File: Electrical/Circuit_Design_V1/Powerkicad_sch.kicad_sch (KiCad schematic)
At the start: 0 parts

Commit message: #3 Creating power sub-schematic.
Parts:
- added C1: 1uF, symbol Device:C
- added P1: ~, symbol Etchasketch_hardware_symbol_library:20mm_Coin_Cell_Breakout_Board_(CR2032)
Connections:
- new net +3V3: C1.2, P1.1 (3V)
- new net GND: C1.1, P1.2 (GND)
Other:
- company: (none) -> AdrianTheHacker
- title: (none) -> Power

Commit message: #3 Sourcing capacitors, and designing power for MCU.
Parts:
- C1: Digikey Part Number (none) -> 3372-0603B105K100XDTR-ND
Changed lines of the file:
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@@
 			)
 		)
-		(property "Datasheet" "https://www.digikey.ca/en/products/detail/nextgen-components/0603B105K250XD/14670931"
+		(property "Datasheet" "https://mm.digikey.com/Volume0/opasdata/d220001/medias/docus/6482/3372_0603B105K100XD.pdf"
 			(at 149.86 113.03 0)
 			(effects
@@
 			)
 		)
-		(property "Description" "0603B105K250XD 1uF Ceramic Capacitor (25V)"
+		(property "Description" "1 µF ±10% 10V Ceramic Capacitor X7R 0603 (1608 Metric)"
 			(at 149.86 113.03 0)
 			(effects
 				(font
+					(size 1.27 1.27)
+				)
+				(hide yes)
+			)
+		)
+		(property "Digikey Part Number" "3372-0603B105K100XDTR-ND"
+			(at 149.86 113.03 90)
+			(effects
+				(font

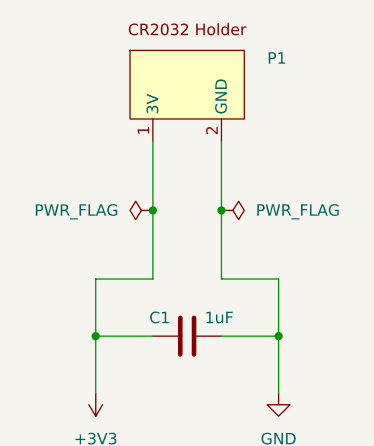
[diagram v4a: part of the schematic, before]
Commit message: #3 Making symbols.
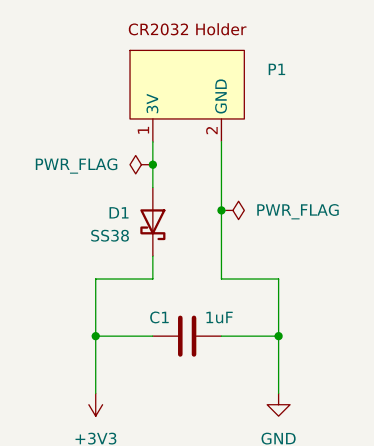
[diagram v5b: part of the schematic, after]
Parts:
- added D1: SS38, Diode_SMD:D_SMA, symbol Diode:SS38
- C1: footprint (none) -> Capacitor_SMD:C_0603_1608Metric
- P1: footprint (none) -> Etchasketch_Footprints:Coincell_Battery_Holder
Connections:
- net +3V3: now also D1.1 (K); no longer P1.1 (3V)
- new net: D1.2 (A), P1.1 (3V)
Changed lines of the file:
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@@
-	)
-	(junction
-		(at 146.05 99.06)
-		(diameter 0)
-		(color 0 0 0 0)
 	)
 	(junction
@@
 	)
 	(junction
+		(at 146.05 93.98)
+		(diameter 0)
+		(color 0 0 0 0)
+	)
+	(junction
 		(at 139.7 113.03)
 		(diameter 0)
@@
 	(wire
 		(pts
+			(xy 146.05 104.14) (xy 146.05 106.68)
+		)
+		(stroke
+			(width 0)
+			(type default)
+		)
+	)
+	(wire
+		(pts
 			(xy 139.7 106.68) (xy 139.7 113.03)
 		)
@@
 	(wire
 		(pts
+			(xy 146.05 93.98) (xy 146.05 91.44)
+		)
+		(stroke
+			(width 0)
+			(type default)
+		)
+	)
+	(wire
+		(pts
 			(xy 160.02 113.03) (xy 160.02 119.38)
 		)
@@
 	(wire
 		(pts
-			(xy 146.05 106.68) (xy 146.05 99.06)
-		)
-		(stroke
-			(width 0)
-			(type default)
-		)
-	)
-	(wire
-		(pts
-			(xy 146.05 99.06) (xy 146.05 91.44)
+			(xy 146.05 93.98) (xy 146.05 96.52)
 		)
 		(stroke
@@
 			)
 		)
-		(property "Footprint" ""
+		(property "Footprint" "Capacitor_SMD:C_0603_1608Metric"
 			(at 146.05 113.9952 0)
 			(effects
@@
 	(symbol
 		(lib_id "power:PWR_FLAG")
-		(at 146.05 99.06 90)
+		(at 146.05 93.98 90)
 		(unit 1)
 		(exclude_from_sim no)
@@
 		(fields_autoplaced yes)
 		(property "Reference" "#FLG01"
-			(at 144.145 99.06 0)
+			(at 144.145 93.98 0)
 			(effects
 				(font
@@
 		)
 		(property "Value" "PWR_FLAG"
-			(at 142.24 99.0599 90)
+			(at 142.24 93.9799 90)
 			(effects
 				(font
@@
 		)
 		(property "Footprint" ""
-			(at 146.05 99.06 0)
+			(at 146.05 93.98 0)
 			(effects
 				(font
@@
 		)
 		(property "Datasheet" "~"
-			(at 146.05 99.06 0)
+			(at 146.05 93.98 0)
 			(effects
 				(font
@@
 		)
 		(property "Description" "Special symbol for telling ERC where power comes from"
-			(at 146.05 99.06 0)
+			(at 146.05 93.98 0)
 			(effects
 				(font
@@
 	)
 	(symbol
+		(lib_id "Etchasketch_hardware_symbol_library:20mm_Coin_Cell_Breakout_Board_(CR2032)")
+		(at 149.86 88.9 0)
+		(unit 1)
+		(exclude_from_sim no)
+		(in_bom yes)
+		(on_board yes)
+		(dnp no)
+		(fields_autoplaced yes)
+		(property "Reference" "P1"
+			(at 158.75 83.4361 0)
+			(effects
+				(font
+					(size 1.27 1.27)
+				)
+				(justify left)
+			)
+		)
+		(property "Value" "~"
+			(at 149.86 88.9 0)
+			(effects
+				(font
+					(size 1.27 1.27)
+				)
+				(hide yes)
+			)
+		)
+		(property "Footprint" "Etchasketch_Footprints:Coincell_Battery_Holder"
+			(at 149.86 88.9 0)
+			(effects
+				(font
+					(size 1.27 1.27)
+				)
+				(hide yes)
+			)
+		)
+		(property "Datasheet" "https://www.te.com/commerce/DocumentDelivery/DDEController?Action=srchrtrv&DocNm=BAT-HLD-001&DocType=Data+Sheet&DocLang=English&DocFormat=pdf&PartCntxt=BAT-HLD-001"
+			(at 150.876 75.946 0)
+			(effects
+				(font
+					(size 1.27 1.27)
+				)
+				(hide yes)
+			)
+		)
+		(property "Description" "Coincell battery holder"
+			(at 149.352 73.406 0)
+			(effects
+				(font
+					(size 1.27 1.27)
+				)
+				(hide yes)
+			)
+		)
+		(pin "1"
+		)
+		(pin "2"
+		)
+		(instances
+			(project ""
+				(path "/40e3562c-f358-42bb-8418-a7c96a575201/7c7c338d-bf18-45a4-ba84-dd266c3ba486"
+					(reference "P1")
+					(unit 1)
+				)
+			)
+		)
+	)
+	(symbol
 		(lib_id "power:GND")
 		(at 160.02 119.38 0)
@@
 				(path "/40e3562c-f358-42bb-8418-a7c96a575201/7c7c338d-bf18-45a4-ba84-dd266c3ba486"
 					(reference "#PWR02")
-					(unit 1)
-				)
-			)
-		)
-	)
-	(symbol
-		(lib_id "Etchasketch_hardware_symbol_library:20mm_Coin_Cell_Breakout_Board_(CR2032)")
-		(at 149.86 88.9 0)
-		(unit 1)
-		(exclude_from_sim no)
-		(in_bom yes)
-		(on_board yes)
-		(dnp no)
-		(fields_autoplaced yes)
-		(property "Reference" "P1"
-			(at 158.75 82.1661 0)
-			(effects
-				(font
-					(size 1.27 1.27)
-				)
-				(justify left)
-			)
-		)
-		(property "Value" "~"
-			(at 158.75 84.7061 0)
-			(effects
-				(font
-					(size 1.27 1.27)
-				)
-				(justify left)
-			)
-		)
-		(property "Footprint" ""
-			(at 149.86 88.9 0)
-			(effects
-				(font
-					(size 1.27 1.27)
-				)
-				(hide yes)
-			)
-		)
-		(property "Datasheet" "https://www.te.com/commerce/DocumentDelivery/DDEController?Action=srchrtrv&DocNm=BAT-HLD-001&DocType=Data+Sheet&DocLang=English&DocFormat=pdf&PartCntxt=BAT-HLD-001"
-			(at 150.876 75.946 0)
-			(effects
-				(font
-					(size 1.27 1.27)
-				)
-				(hide yes)
-			)
-		)
-		(property "Description" "Coincell battery holder"
-			(at 149.352 73.406 0)
-			(effects
-				(font
-					(size 1.27 1.27)
-				)
-				(hide yes)
-			)
-		)
-		(pin "1"
-		)
-		(pin "2"
-		)
-		(instances
-			(project ""
-				(path "/40e3562c-f358-42bb-8418-a7c96a575201/7c7c338d-bf18-45a4-ba84-dd266c3ba486"
-					(reference "P1")
 					(unit 1)
 				)
@@
 					(unit 1)
 				)
+			)
+		)
+	)
+	(symbol
+		(lib_id "Diode:SS38")
+		(at 146.05 100.33 270)
+		(mirror x)
+		(unit 1)
+		(exclude_from_sim no)
+		(in_bom yes)
+		(on_board yes)
+		(dnp no)
+		(property "Reference" "D1"
+			(at 143.51 99.3774 90)
+			(effects
+				(font
+					(size 1.27 1.27)
+				)
+				(justify right)
+			)
+		)
+		(property "Value" "SS38"
+			(at 143.51 101.9174 90)
+			(effects
+				(font
+					(size 1.27 1.27)
+				)
+				(justify right)
+			)
+		)
+		(property "Footprint" "Diode_SMD:D_SMA"
+			(at 141.605 100.33 0)
+			(effects
+				(font
+					(size 1.27 1.27)
+				)
+				(hide yes)
+			)
+		)
+		(property "Datasheet" "https://www.microdiode.com/uploadfiles//PDF/SS32-THRU-SS3200-SMA.pdf"
+			(at 146.05 100.33 0)
+			(effects
+				(font
+					(size 1.27 1.27)
+				)
+				(hide yes)
+			)
+		)
+		(property "Description" "80V 3A Schottky Diode, SMA"
+			(at 146.05 100.33 0)
+			(effects
+				(font
+					(size 1.27 1.27)
+				)
+				(hide yes)
+			)
+		)
+		(pin "2"
+		)
+		(pin "1"
+		)
+		(instances
+			(project ""
+				(path "/40e3562c-f358-42bb-8418-a7c96a575201/7c7c338d-bf18-45a4-ba84-dd266c3ba486"
+					(reference "D1")
+					(unit 1)
+				)

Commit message: #3 Finishing some circuitry.
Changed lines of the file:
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@@
 	)
 	(junction
-		(at 153.67 99.06)
+		(at 153.67 93.98)
 		(diameter 0)
 		(color 0 0 0 0)
@@
 	(wire
 		(pts
-			(xy 153.67 99.06) (xy 153.67 91.44)
+			(xy 153.67 93.98) (xy 153.67 91.44)
 		)
 		(stroke
@@
 	(wire
 		(pts
-			(xy 153.67 106.68) (xy 153.67 99.06)
+			(xy 153.67 93.98) (xy 153.67 106.68)
 		)
 		(stroke
@@
 	(symbol
 		(lib_id "power:PWR_FLAG")
-		(at 153.67 99.06 270)
+		(at 153.67 93.98 270)
 		(unit 1)
 		(exclude_from_sim no)
@@
 		(fields_autoplaced yes)
 		(property "Reference" "#FLG02"
-			(at 155.575 99.06 0)
+			(at 155.575 93.98 0)
 			(effects
 				(font
@@
 		)
 		(property "Value" "PWR_FLAG"
-			(at 157.48 99.0599 90)
+			(at 157.48 93.9799 90)
 			(effects
 				(font
@@
 		)
 		(property "Footprint" ""
-			(at 153.67 99.06 0)
+			(at 153.67 93.98 0)
 			(effects
 				(font
@@
 		)
 		(property "Datasheet" "~"
-			(at 153.67 99.06 0)
+			(at 153.67 93.98 0)
 			(effects
 				(font
@@
 		)
 		(property "Description" "Special symbol for telling ERC where power comes from"
-			(at 153.67 99.06 0)
-			(effects
-				(font
+			(at 153.67 93.98 0)
+			(effects
+				(font

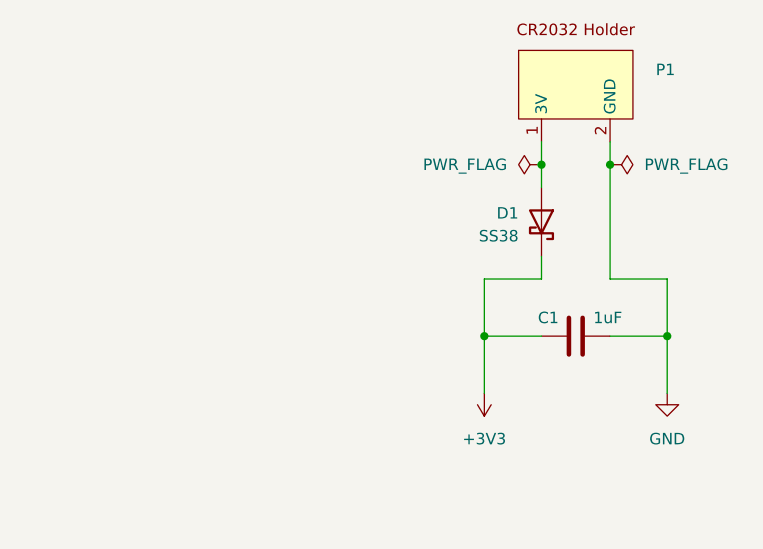
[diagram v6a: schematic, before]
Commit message: Completing schematic.
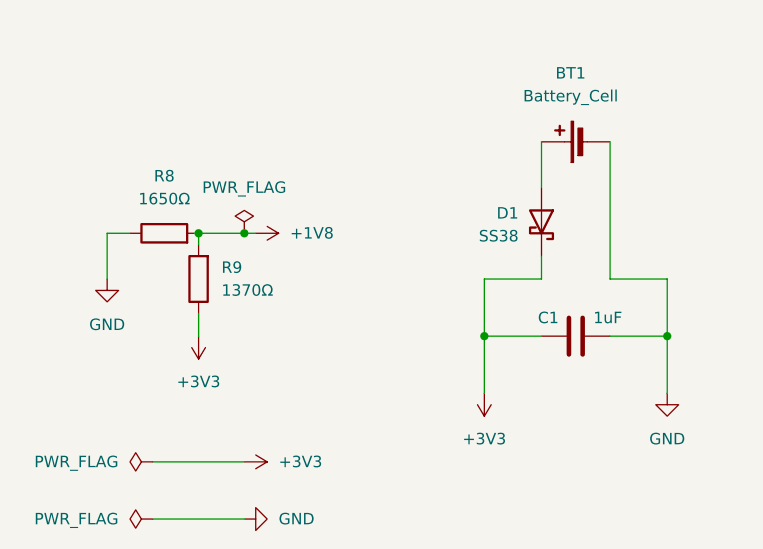
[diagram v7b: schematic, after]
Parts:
- removed P1: ~, Etchasketch_Footprints:Coincell_Battery_Holder, symbol Etchasketch_hardware_symbol_library:20mm_Coin_Cell_Breakout_Board_(CR2032)
- added BT1: Battery_Cell, Etchasketch_Footprints:Coincell_Battery_Holder, symbol Device:Battery_Cell
- added R8: 1650Ω, Resistor_SMD:R_0805_2012Metric, symbol Device:R
- added R9: 1370Ω, Resistor_SMD:R_0805_2012Metric, symbol Device:R
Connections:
- net +3V3: now also R9.1
- net GND: now also BT1.2 (-), R8.1
- net at D1.2 (A): now also BT1.1 (+)
- new net +1V8: R8.2, R9.2
